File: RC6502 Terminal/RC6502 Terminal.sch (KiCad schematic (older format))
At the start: 40 parts, among them J1 RC6502_Backplane, J2 KBD_SER, J3 VID_SER, J4 KBD_ICSP, J5 VID_ICSP, J6 AUDIO, J7 VIDEO, J8 Keyboard, SW1 KBD_RES, SW2 VID_RES, U1 MC6821, U2 74LS138, U3 74LS00, U4 ATMEGA328_MCU, U5 ATMEGA328_MCU, Y1 16Mhz, Y2 16Mhz

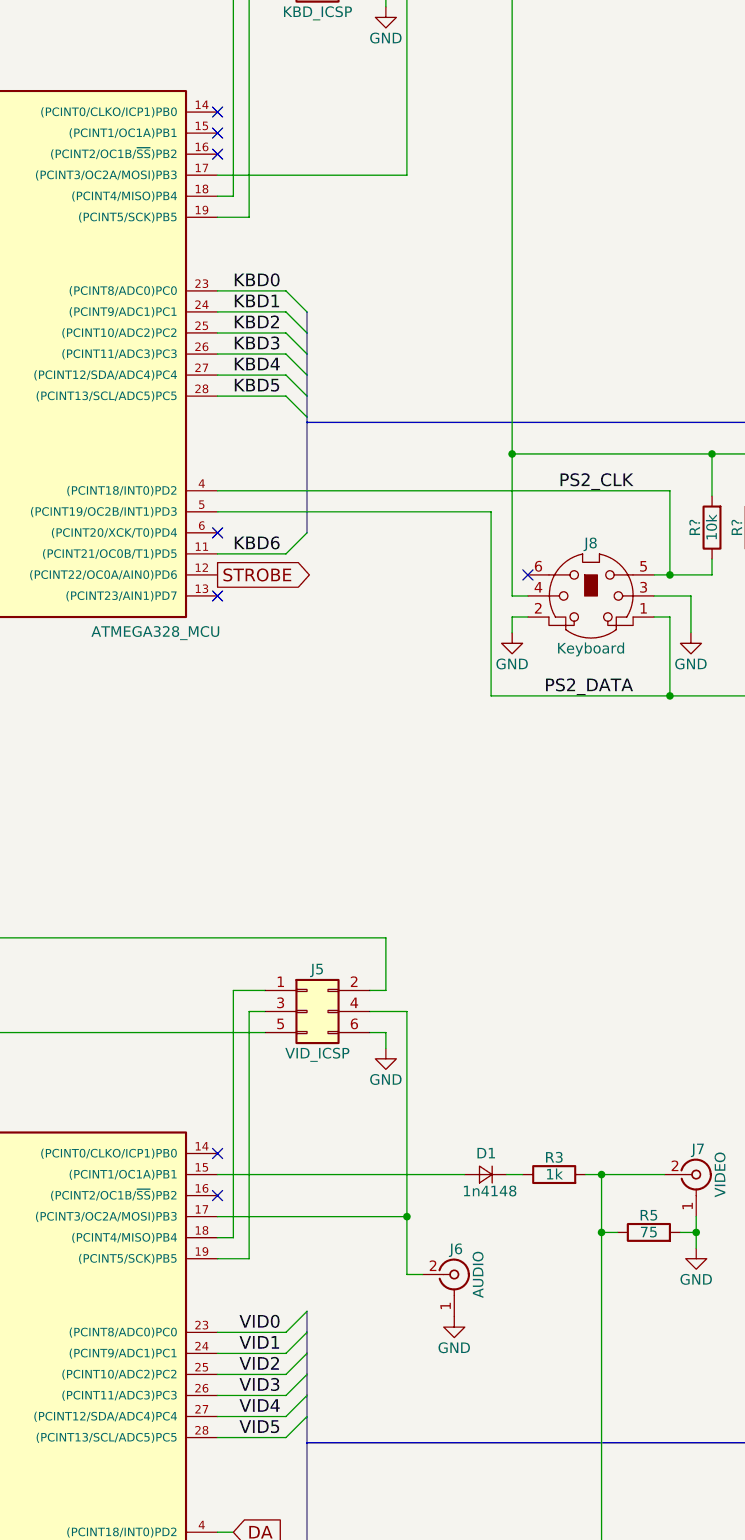
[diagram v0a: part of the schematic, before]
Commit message: Added LEDs
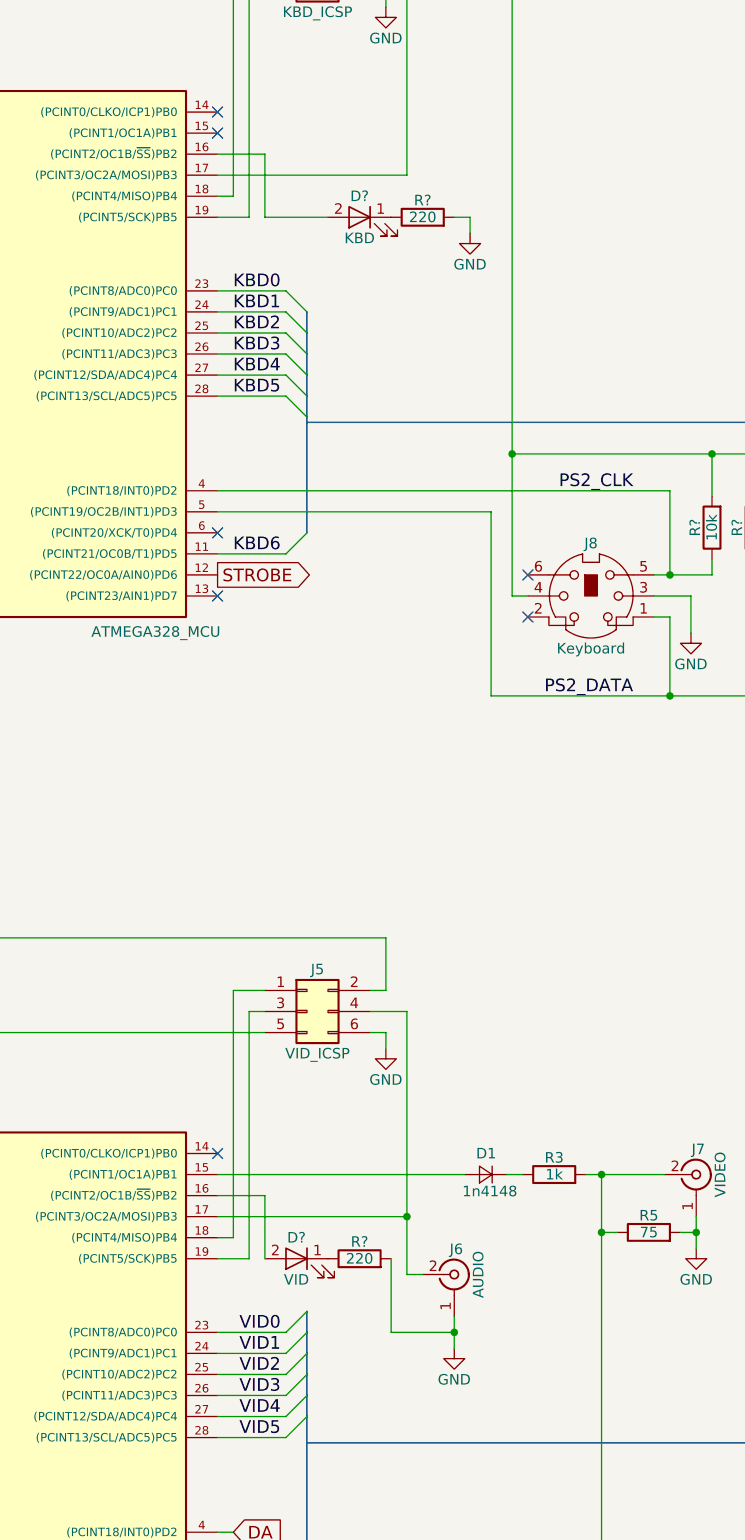
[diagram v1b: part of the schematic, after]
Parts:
- added D?: VID, symbol LED
- added D?: KBD, symbol LED
- added R? (x2): 220, symbol R
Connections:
- net GND: now also R?.2, R?.2; no longer J8.2
- net at U4.16 ((PCINT2/OC1B/~SS~)PB2): now also D?.2 (A)
- net at U5.16 ((PCINT2/OC1B/~SS~)PB2): now also D?.2 (A)
- new net: D?.1 (K), R?.1 (x2)
- no-connect marks 44 -> 43
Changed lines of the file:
@@
 $EndComp
 NoConn ~ 4550 2675
-NoConn ~ 4550 2875
 NoConn ~ 4550 4675
 $Comp
@@
 L GND #PWR023
 U 1 1 5E27D914
-P 5675 8400
-F 0 "#PWR023" H 5675 8150 50  0001 C CNN
-F 1 "GND" H 5675 8250 50  0000 C CNN
-F 2 "" H 5675 8400 50  0001 C CNN
-F 3 "" H 5675 8400 50  0001 C CNN
-	1    5675 8400
+P 5675 8550
+F 0 "#PWR023" H 5675 8300 50  0001 C CNN
+F 1 "GND" H 5675 8400 50  0000 C CNN
+F 2 "" H 5675 8550 50  0001 C CNN
+F 3 "" H 5675 8550 50  0001 C CNN
+	1    5675 8550
 	1    0    0    -1
 $EndComp
@@
 $EndComp
 NoConn ~ 4550 7625
-NoConn ~ 4550 7825
 NoConn ~ 4550 9625
 NoConn ~ 4550 9825
@@
 Text Label 6525 5450 2    60   ~ 0
 PS2_DATA
-$Comp
-L GND #PWR030
-U 1 1 5E2A3505
-P 5950 5150
-F 0 "#PWR030" H 5950 4900 50  0001 C CNN
-F 1 "GND" H 5950 5000 50  0000 C CNN
-F 2 "" H 5950 5150 50  0001 C CNN
-F 3 "" H 5950 5150 50  0001 C CNN
-	1    5950 5150
-	-1   0    0    -1
-$EndComp
-Wire Wire Line
-	6025 5075 5950 5075
-Wire Wire Line
-	5950 5075 5950 5150
 Wire Wire Line
 	6625 5075 6700 5075
@@
 	7100 4300 7100 4500
 Connection ~ 6900 4300
+NoConn ~ 6025 5075
+$Comp
+L LED D?
+U 1 1 5E2B88B6
+P 4925 8125
+F 0 "D?" H 4925 8225 50  0000 C CNN
+F 1 "VID" H 4925 8025 50  0000 C CNN
+F 2 "" H 4925 8125 50  0001 C CNN
+F 3 "" H 4925 8125 50  0001 C CNN
+	1    4925 8125
+	-1   0    0    -1
+$EndComp
+$Comp
+L R R?
+U 1 1 5E2B8CE9
+P 5225 8125
+F 0 "R?" V 5305 8125 50  0000 C CNN
+F 1 "220" V 5225 8125 50  0000 C CNN
+F 2 "" V 5155 8125 50  0001 C CNN
+F 3 "" H 5225 8125 50  0001 C CNN
+	1    5225 8125
+	0    -1   -1   0
+$EndComp
+Wire Wire Line
+	4550 7825 4775 7825
+Wire Wire Line
+	4775 7825 4775 8125
+Wire Wire Line
+	5675 8550 5675 8400
+Wire Wire Line
+	5375 8125 5375 8475
+Wire Wire Line
+	5375 8475 5675 8475
+Connection ~ 5675 8475
+$Comp
+L LED D?
+U 1 1 5E2BB703
+P 5225 3175
+F 0 "D?" H 5225 3275 50  0000 C CNN
+F 1 "KBD" H 5225 3075 50  0000 C CNN
+F 2 "" H 5225 3175 50  0001 C CNN
+F 3 "" H 5225 3175 50  0001 C CNN
+	1    5225 3175
+	-1   0    0    -1
+$EndComp
+$Comp
+L R R?
+U 1 1 5E2BB709
+P 5525 3175
+F 0 "R?" V 5605 3175 50  0000 C CNN
+F 1 "220" V 5525 3175 50  0000 C CNN
+F 2 "" V 5455 3175 50  0001 C CNN
+F 3 "" H 5525 3175 50  0001 C CNN
+	1    5525 3175
+	0    -1   -1   0
+$EndComp
+Wire Wire Line
+	4550 2875 4775 2875
+Wire Wire Line
+	4775 2875 4775 3175
+Wire Wire Line
+	4775 3175 5075 3175
+Wire Wire Line
+	5675 3175 5750 3175
+Wire Wire Line
+	5750 3175 5750 3250
+$Comp
+L GND #PWR?
+U 1 1 5E2BC015
+P 5750 3250
+F 0 "#PWR?" H 5750 3000 50  0001 C CNN
+F 1 "GND" H 5750 3100 50  0000 C CNN
+F 2 "" H 5750 3250 50  0001 C CNN
+F 3 "" H 5750 3250 50  0001 C CNN
+	1    5750 3250
+	1    0    0    -1
+$EndComp
 $EndSCHEMATC

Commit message: Assigned footprints
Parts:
- C1, C10, C11, C12, C2, C3, C4, C5, C6, C7, C8, C9: footprint (none) -> Capacitors_THT:C_Disc_D4.7mm_W2.5mm_P5.00mm
- D1, D2: footprint (none) -> Diodes_THT:D_DO-35_SOD27_P7.62mm_Horizontal
- D3, D4: renamed from D?; footprint (none) -> LEDs:LED_D5.0mm
- J1: footprint (none) -> Pin_Headers:Pin_Header_Angled_1x39_Pitch2.54mm
- J2, J3: footprint (none) -> Pin_Headers:Pin_Header_Angled_1x06_Pitch2.54mm
- J4, J5: footprint (none) -> Pin_Headers:Pin_Header_Straight_2x03_Pitch2.54mm
- J6, J7: footprint (none) -> rca:rca_yellow
- J8: footprint (none) -> ps2:MINI-DIN-6-FULL-SHIELD; symbol Mini-DIN-6 -> PS/2_Connector
- JP1, JP2: footprint (none) -> Pin_Headers:Pin_Header_Straight_1x02_Pitch2.54mm
- R1, R2, R3, R4, R5: footprint (none) -> Resistors_THT:R_Axial_DIN0207_L6.3mm_D2.5mm_P10.16mm_Horizontal
- R6, R7, R8, R9: renamed from R?; footprint (none) -> Resistors_THT:R_Axial_DIN0207_L6.3mm_D2.5mm_P10.16mm_Horizontal
- SW1, SW2: footprint (none) -> Buttons_Switches_THT:SW_PUSH_6mm
- U1: footprint (none) -> Housings_DIP:DIP-40_W15.24mm_Socket_LongPads
- U2: footprint (none) -> Housings_DIP:DIP-16_W7.62mm_Socket_LongPads
- U3: footprint (none) -> Housings_DIP:DIP-14_W7.62mm_Socket_LongPads
- U4, U5: footprint DIL28 -> Housings_DIP:DIP-28_W7.62mm_Socket_LongPads
- Y1, Y2: footprint (none) -> Crystals:Crystal_HC49-4H_Vertical
